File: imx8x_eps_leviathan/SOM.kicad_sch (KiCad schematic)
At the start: 33 parts, among them J10 BTH-070-02-L-D-A, J9 BTH-070-02-L-D-A

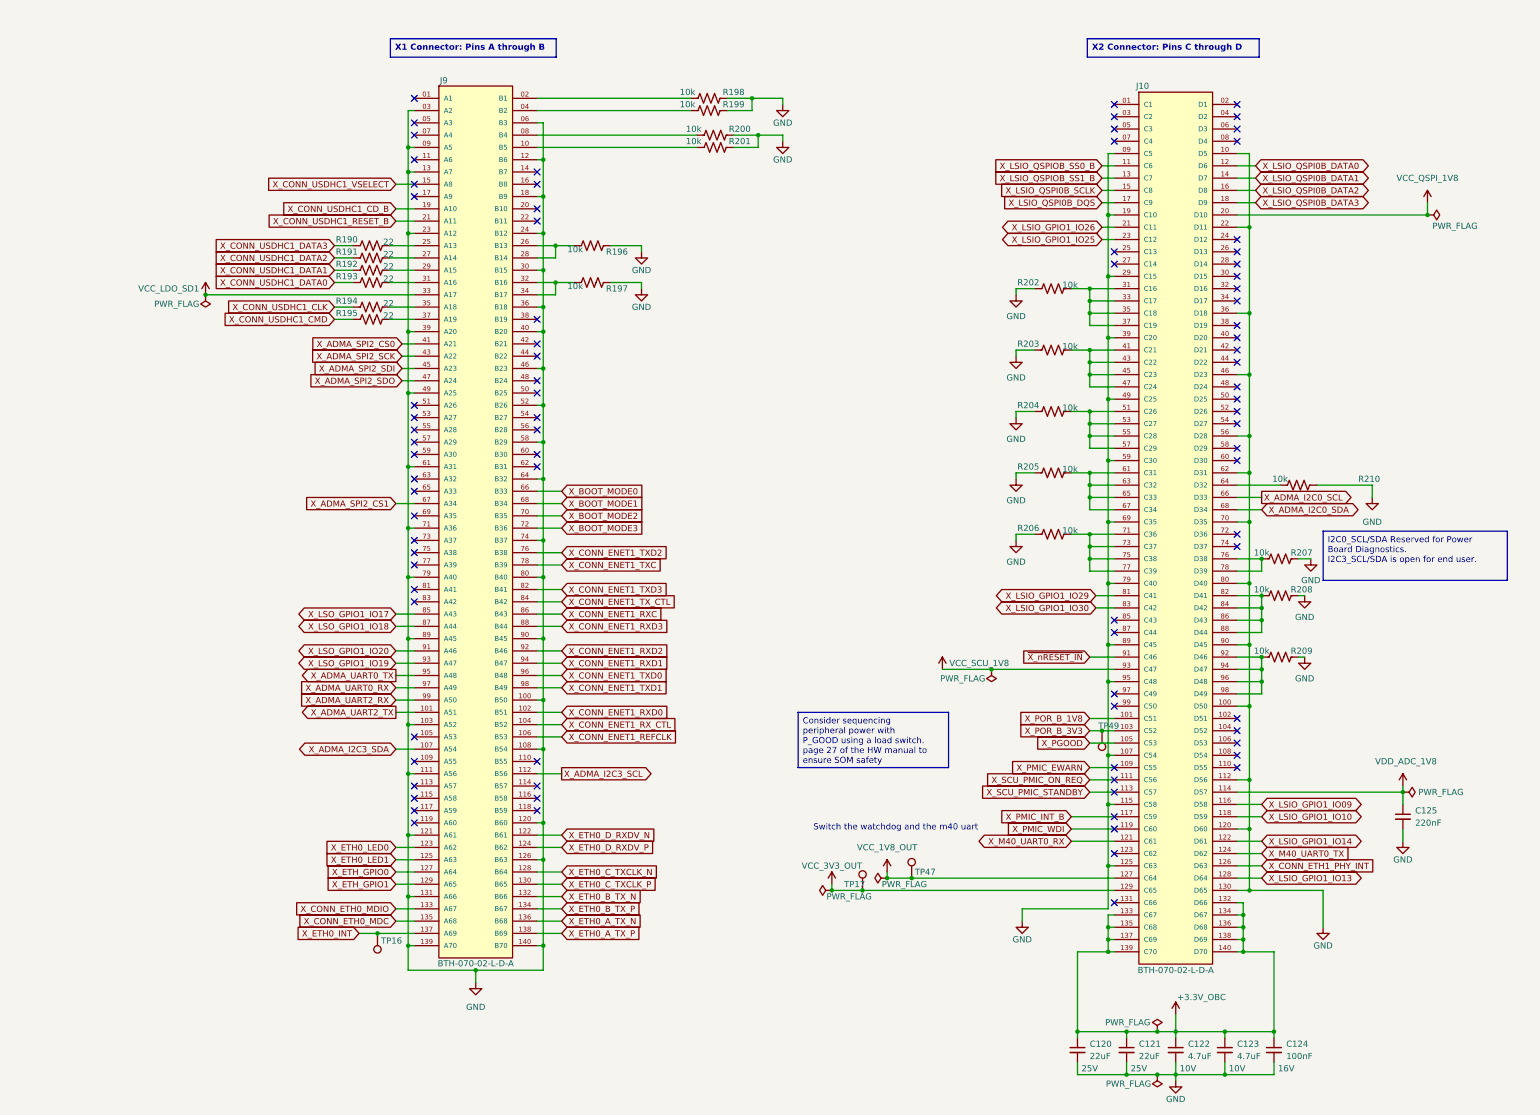
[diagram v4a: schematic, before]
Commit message: Schematic Need Double Checking, But I think its done
I think ive finished adding every change we wanted to include after the merging along with all the changes requested by PHYTEC. I would like to sit down and review the muxing configuration and double check every single sheet to make sure its perfect. then we can send it off to Phytec.
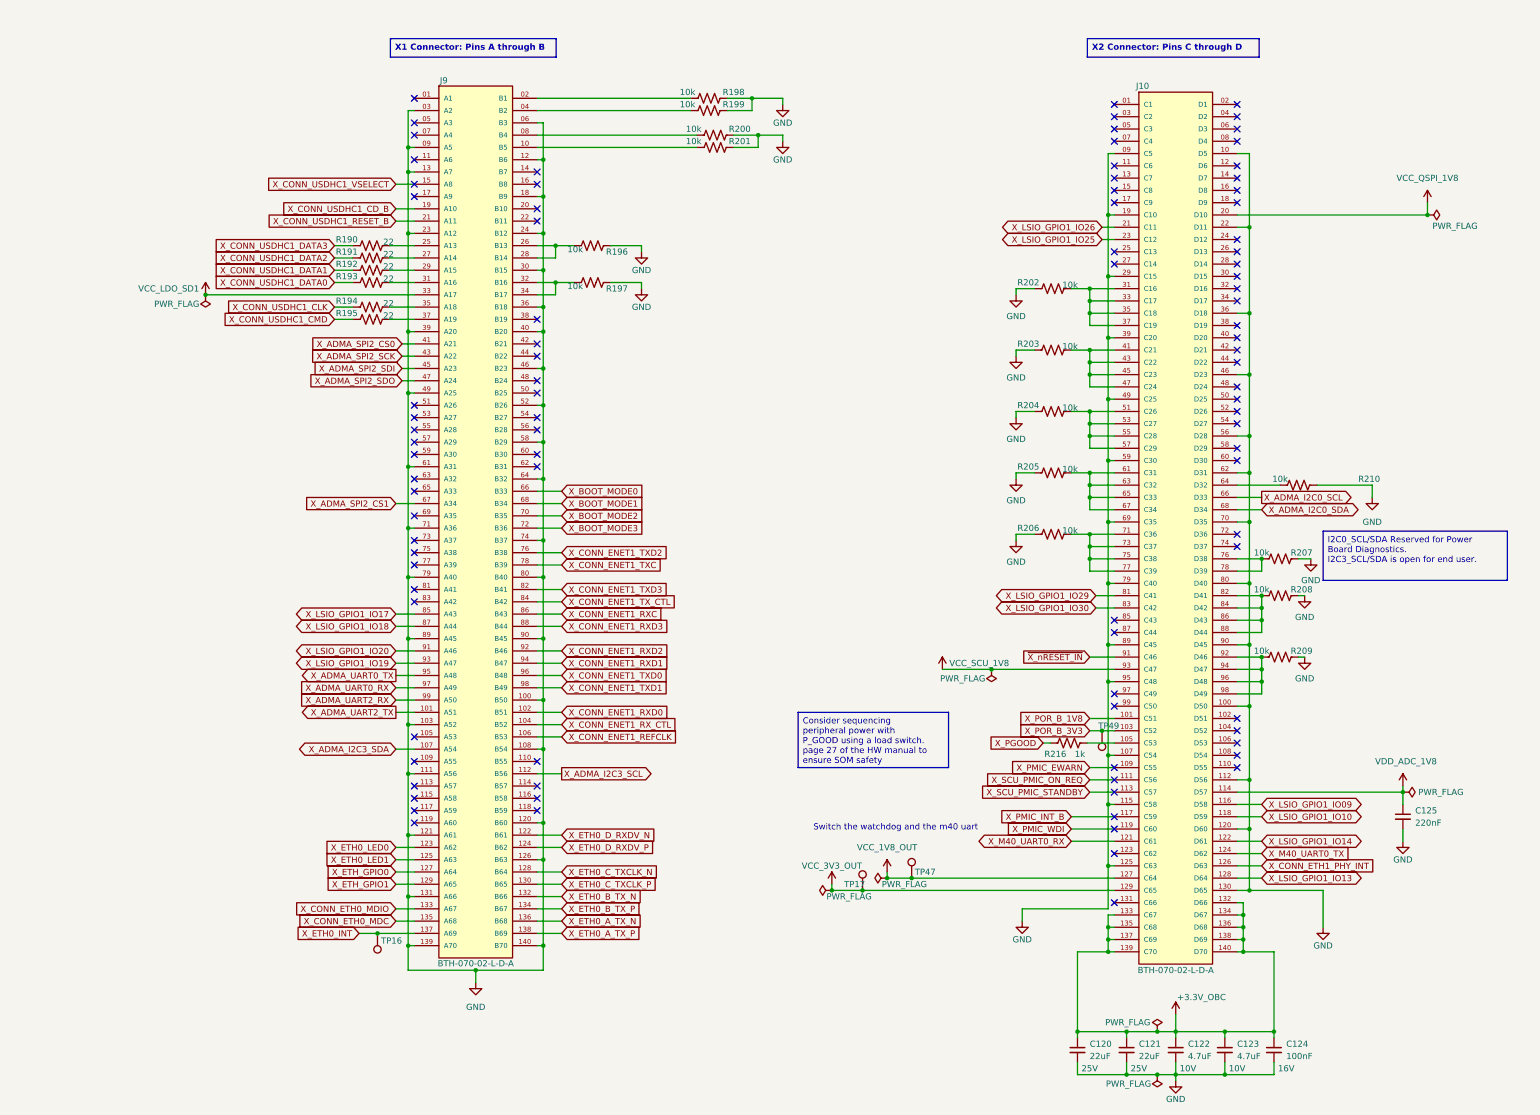
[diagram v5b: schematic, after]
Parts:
- added R216: 1k, EPS:R0402, symbol Device:R_US
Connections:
- net X_PGOOD: now also R216.1; no longer J10.105 (C53)
- net X_LSIO_QSPI0B_DATA0: no longer names the net of J10.12 (D6)
- net X_LSIO_QSPI0B_DATA1: no longer names the net of J10.14 (D7)
- net X_LSIO_QSPI0B_DATA2: no longer names the net of J10.16 (D8)
- net X_LSIO_QSPI0B_DATA3: no longer names the net of J10.18 (D9)
- net X_LSIO_QSPI0B_DQS: no longer names the net of J10.17 (C9)
- net X_LSIO_QSPI0B_SCLK: no longer names the net of J10.15 (C8)
- net X_LSIO_QSPIOB_SS0_B: no longer names the net of J10.11 (C6)
- net X_LSIO_QSPIOB_SS1_B: no longer names the net of J10.13 (C7)
- net X_LSO_GPIO1_IO17 renamed X_LSIO_GPIO1_IO17
- net X_LSO_GPIO1_IO18 renamed X_LSIO_GPIO1_IO18
- net X_LSO_GPIO1_IO19 renamed X_LSIO_GPIO1_IO19
- net X_LSO_GPIO1_IO20 renamed X_LSIO_GPIO1_IO20
- new net: J10.105 (C53), R216.2
- no-connect marks 86 -> 94

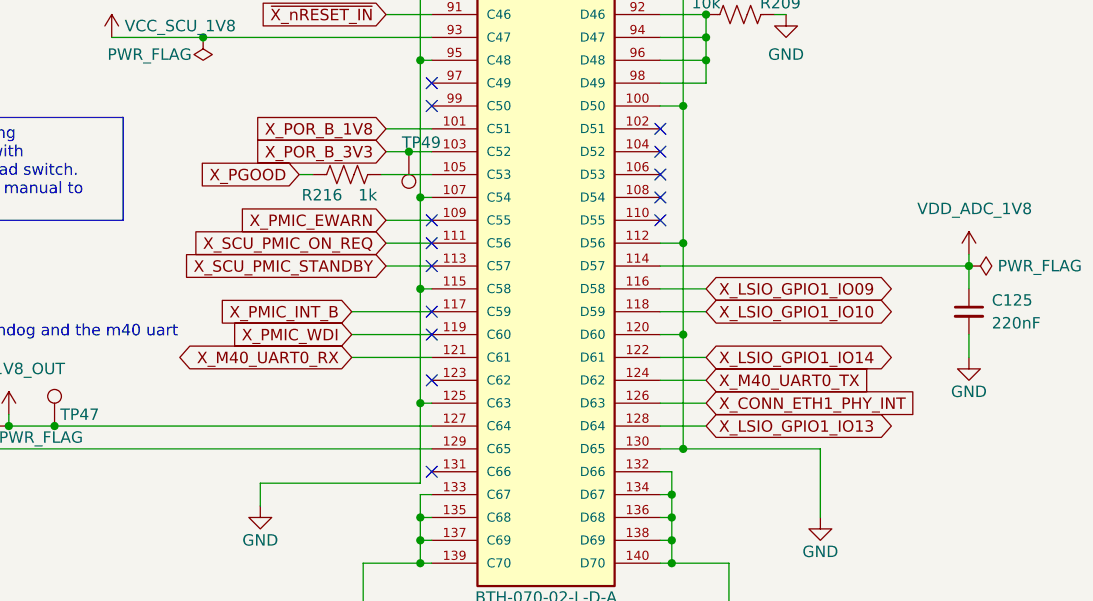
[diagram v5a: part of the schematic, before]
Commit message: Schematic Complete. Ready for Phytec.
Fixed muxing with a few things that were missing with ETH1, and corrected some missing labels. Ready for Phytecs review.
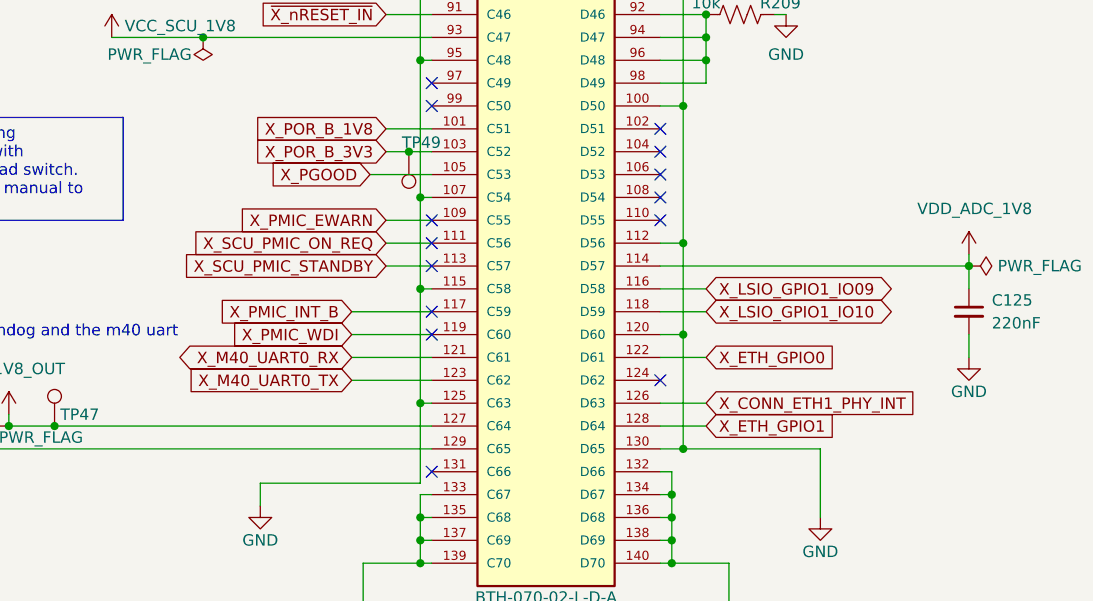
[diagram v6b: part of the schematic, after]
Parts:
- removed R216: 1k, EPS:R0402, symbol Device:R_US
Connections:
- net X_LSIO_GPIO1_IO13 is gone; now on net X_ETH_GPIO1: J10.128 (D64)
- net X_LSIO_GPIO1_IO14 is gone; now on net X_ETH_GPIO0: J10.122 (D61)
- net X_M40_UART0_TX: now also J10.123 (C62); no longer J10.124 (D62)
- net X_PGOOD: now also J10.105 (C53)
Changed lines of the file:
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@@
 	)
 	(no_connect
-		(at 266.192 195.072)
-	)
-	(no_connect
 		(at 291.592 167.132)
 	)
@@
 	)
 	(no_connect
+		(at 291.592 195.072)
+	)
+	(no_connect
 		(at 291.592 106.172)
 	)
@@
 	(wire
 		(pts
-			(xy 251.46 172.212) (xy 252.984 172.212)
+			(xy 259.334 172.212) (xy 266.192 172.212)
 		)
 		(stroke
@@
 	(wire
 		(pts
-			(xy 260.604 172.212) (xy 266.192 172.212)
-		)
-		(stroke
-			(width 0)
-			(type default)
-		)
-	)
-	(wire
-		(pts
 			(xy 264.922 62.992) (xy 266.192 62.992)
 		)
@@
 	(wire
 		(pts
-			(xy 291.592 195.072) (xy 296.672 195.072)
-		)
-		(stroke
-			(width 0)
-			(type default)
-		)
-	)
-	(wire
-		(pts
 			(xy 120.142 115.062) (xy 120.142 127.762)
 		)
@@
 	(wire
 		(pts
+			(xy 257.302 195.072) (xy 266.192 195.072)
+		)
+		(stroke
+			(width 0)
+			(type default)
+		)
+	)
+	(wire
+		(pts
 			(xy 148.082 102.362) (xy 148.082 109.982)
 		)
@@
 		)
 	)
+	(global_label "X_ETH_GPIO0"
+		(shape input)
+		(at 296.672 192.532 0)
+		(fields_autoplaced yes)
+		(effects
+			(font
+				(size 1.27 1.27)
+			)
+			(justify left)
+		)
+		(property "Intersheetrefs" "${INTERSHEET_REFS}"
+			(at 311.9338 192.532 0)
+			(effects
+				(font
+					(size 1.27 1.27)
+				)
+				(justify left)
+				(hide yes)
+			)
+		)
+	)
 	(global_label "X_ETH0_A_TX_N"
 		(shape input)
@@
 	(global_label "X_PGOOD"
 		(shape input)
-		(at 251.46 172.212 180)
+		(at 259.334 172.212 180)
 		(fields_autoplaced yes)
 		(effects
@@
 		)
 		(property "Intersheetrefs" "${INTERSHEET_REFS}"
-			(at 239.8267 172.212 0)
+			(at 247.7007 172.212 0)
 			(effects
 				(font
@@
 		)
 	)
-	(global_label "X_LSIO_GPIO1_IO14"
-		(shape bidirectional)
-		(at 296.672 192.532 0)
+	(global_label "X_CONN_USDHC1_CMD"
+		(shape input)
+		(at 104.902 84.582 180)
 		(fields_autoplaced yes)
 		(effects
@@
 				(size 1.27 1.27)
 			)
-			(justify left)
+			(justify right)
 		)
 		(property "Intersheetrefs" "${INTERSHEET_REFS}"
-			(at 319.0928 192.532 0)
+			(at 80.9316 84.582 0)
 			(effects
 				(font
 					(size 1.27 1.27)
 				)
-				(justify left)
+				(justify right)
 				(hide yes)
 			)
 		)
 	)
-	(global_label "X_CONN_USDHC1_CMD"
+	(global_label "X_SCU_PMIC_STANDBY"
 		(shape input)
-		(at 104.902 84.582 180)
+		(at 261.112 182.372 180)
 		(fields_autoplaced yes)
 		(effects
@@
 		)
 		(property "Intersheetrefs" "${INTERSHEET_REFS}"
-			(at 80.9316 84.582 0)
+			(at 237.3835 182.372 0)
 			(effects
 				(font
@@
 		)
 	)
-	(global_label "X_SCU_PMIC_STANDBY"
-		(shape input)
-		(at 261.112 182.372 180)
+	(global_label "X_LSIO_GPIO1_IO26"
+		(shape bidirectional)
+		(at 263.652 65.532 180)
 		(fields_autoplaced yes)
 		(effects
@@
 		)
 		(property "Intersheetrefs" "${INTERSHEET_REFS}"
-			(at 237.3835 182.372 0)
+			(at 241.2312 65.532 0)
 			(effects
 				(font
@@
 		)
 	)
-	(global_label "X_LSIO_GPIO1_IO26"
-		(shape bidirectional)
-		(at 263.652 65.532 180)
+	(global_label "X_ETH_GPIO1"
+		(shape input)
+		(at 296.672 200.152 0)
 		(fields_autoplaced yes)
 		(effects
@@
 				(size 1.27 1.27)
 			)
-			(justify right)
+			(justify left)
 		)
 		(property "Intersheetrefs" "${INTERSHEET_REFS}"
-			(at 241.2312 65.532 0)
+			(at 311.9338 200.152 0)
 			(effects
 				(font
 					(size 1.27 1.27)
 				)
-				(justify right)
+				(justify left)
 				(hide yes)
 			)
@@
 		)
 	)
-	(global_label "X_LSIO_GPIO1_IO13"
-		(shape bidirectional)
-		(at 296.672 200.152 0)
-		(fields_autoplaced yes)
-		(effects
-			(font
-				(size 1.27 1.27)
-			)
-			(justify left)
-		)
-		(property "Intersheetrefs" "${INTERSHEET_REFS}"
-			(at 319.0928 200.152 0)
-			(effects
-				(font
-					(size 1.27 1.27)
-				)
-				(justify left)
-				(hide yes)
-			)
-		)
-	)
 	(global_label "X_ETH0_A_TX_P"
 		(shape input)
@@
 	(global_label "X_M40_UART0_TX"
 		(shape input)
-		(at 296.672 195.072 0)
+		(at 257.302 195.072 180)
 		(fields_autoplaced yes)
 		(effects
@@
 				(size 1.27 1.27)
 			)
-			(justify left)
+			(justify right)
 		)
 		(property "Intersheetrefs" "${INTERSHEET_REFS}"
-			(at 315.6832 195.072 0)
+			(at 238.2908 195.072 0)
 			(effects
 				(font
 					(size 1.27 1.27)
 				)
-				(justify left)
+				(justify right)
 				(hide yes)
 			)
@@
 					(unit 1)
 				)
-			)
-		)
-	)
-	(symbol
-		(lib_id "Device:R_US")
-		(at 256.794 172.212 90)
-		(unit 1)
-		(exclude_from_sim no)
-		(in_bom yes)
-		(on_board yes)
-		(dnp no)
-		(property "Reference" "R216"
-			(at 254 174.498 90)
-			(effects
-				(font
-					(size 1.27 1.27)
-				)
-			)
-		)
-		(property "Value" "1k"
-			(at 259.08 174.498 90)
-			(effects
-				(font
-					(size 1.27 1.27)
-				)
-			)
-		)
-		(property "Footprint" "EPS:R0402"
-			(at 257.048 171.196 90)
-			(effects
-				(font
-					(size 1.27 1.27)
-				)
-				(hide yes)
-			)
-		)
-		(property "Datasheet" "~"
-			(at 256.794 172.212 0)
-			(effects
-				(font
-					(size 1.27 1.27)
-				)
-				(hide yes)
-			)
-		)
-		(property "Description" "Resistor, US symbol"
-			(at 256.794 172.212 0)
-			(effects
-				(font
-					(size 1.27 1.27)
-				)
-				(hide yes)
-			)
-		)
-		(pin "1"
-		)
-		(pin "2"
-		)
-		(instances
-			(project ""
-				(path "/bd3af9f3-19df-4a2f-8b54-98c48cea082e/1b5b2e76-614d-4307-9232-e06f7c77302d/d76dd75e-585c-4f61-92c5-bda4099b5574"
-					(reference "R216")
-					(unit 1)
-				)

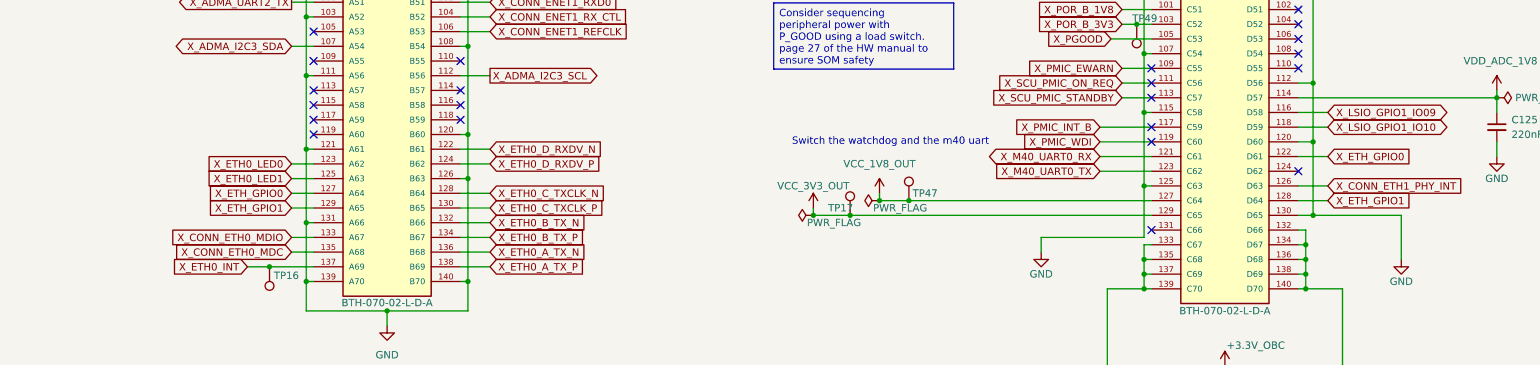
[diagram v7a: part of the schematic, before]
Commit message: Fixed the changes from Phytec
Fixed the issues from the most recent phytec review. Need to still go through the older fixes before the board was merged. This is currently up to date for the what I think is the minimum configuration and use ability.

Thing to note is that there is still a few different sheets that I think need to be added but the major functinallity is there.
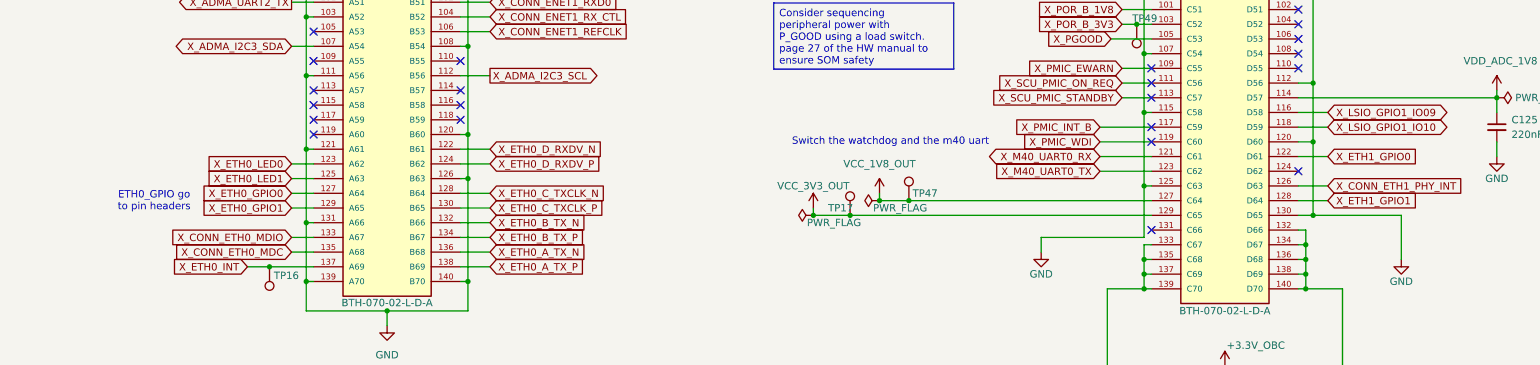
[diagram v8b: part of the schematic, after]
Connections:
- net X_ETH_GPIO0 renamed X_ETH0_GPIO0
- net X_ETH0_GPIO0: no longer J10.122 (D61)
- net X_ETH_GPIO1 renamed X_ETH0_GPIO1
- net X_ETH0_GPIO1: no longer J10.128 (D64)
- new net X_ETH1_GPIO0: J10.122 (D61)
- new net X_ETH1_GPIO1: J10.128 (D64)
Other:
- note added: "ETH0_GPIO go to pin headers"
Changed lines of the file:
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@@
 		(comment 1 "By Luca Lanzillotta & John Pollack")
 	)
+	(text "ETH0_GPIO go \nto pin headers"
+		(exclude_from_sim no)
+		(at 93.726 200.152 0)
+		(effects
+			(font
+				(size 1.27 1.27)
+			)
+		)
+	)
 	(text "Switch the watchdog and the m40 uart"
 		(exclude_from_sim no)
@@
 		)
 	)
-	(global_label "X_ETH_GPIO1"
+	(global_label "X_ETH0_GPIO1"
 		(shape input)
 		(at 117.475 201.295 180)
@@
 		)
 		(property "Intersheetrefs" "${INTERSHEET_REFS}"
-			(at 102.2132 201.295 0)
+			(at 101.0037 201.295 0)
 			(effects
 				(font
@@
 		)
 	)
-	(global_label "X_ETH_GPIO0"
+	(global_label "X_ETH1_GPIO0"
 		(shape input)
 		(at 296.545 192.405 0)
@@
 		)
 		(property "Intersheetrefs" "${INTERSHEET_REFS}"
-			(at 311.8068 192.405 0)
+			(at 313.0163 192.405 0)
 			(effects
 				(font
@@
 		)
 	)
-	(global_label "X_ETH_GPIO1"
+	(global_label "X_ETH1_GPIO1"
 		(shape input)
 		(at 296.545 200.025 0)
@@
 		)
 		(property "Intersheetrefs" "${INTERSHEET_REFS}"
-			(at 311.8068 200.025 0)
+			(at 313.0163 200.025 0)
 			(effects
 				(font
@@
 		)
 	)
-	(global_label "X_ETH_GPIO0"
+	(global_label "X_ETH0_GPIO0"
 		(shape input)
 		(at 117.475 198.755 180)
@@
 		)
 		(property "Intersheetrefs" "${INTERSHEET_REFS}"
-			(at 102.2132 198.755 0)
+			(at 101.0037 198.755 0)
 			(effects
 				(font
